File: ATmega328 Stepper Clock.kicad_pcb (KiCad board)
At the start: 2 copper layers, 9 parts, among them IC1 ATMEGA328-AU, J1 Conn_01x04_Pin, J2 SBH11-PBPC-D05-ST-BK, Y1 Crystal

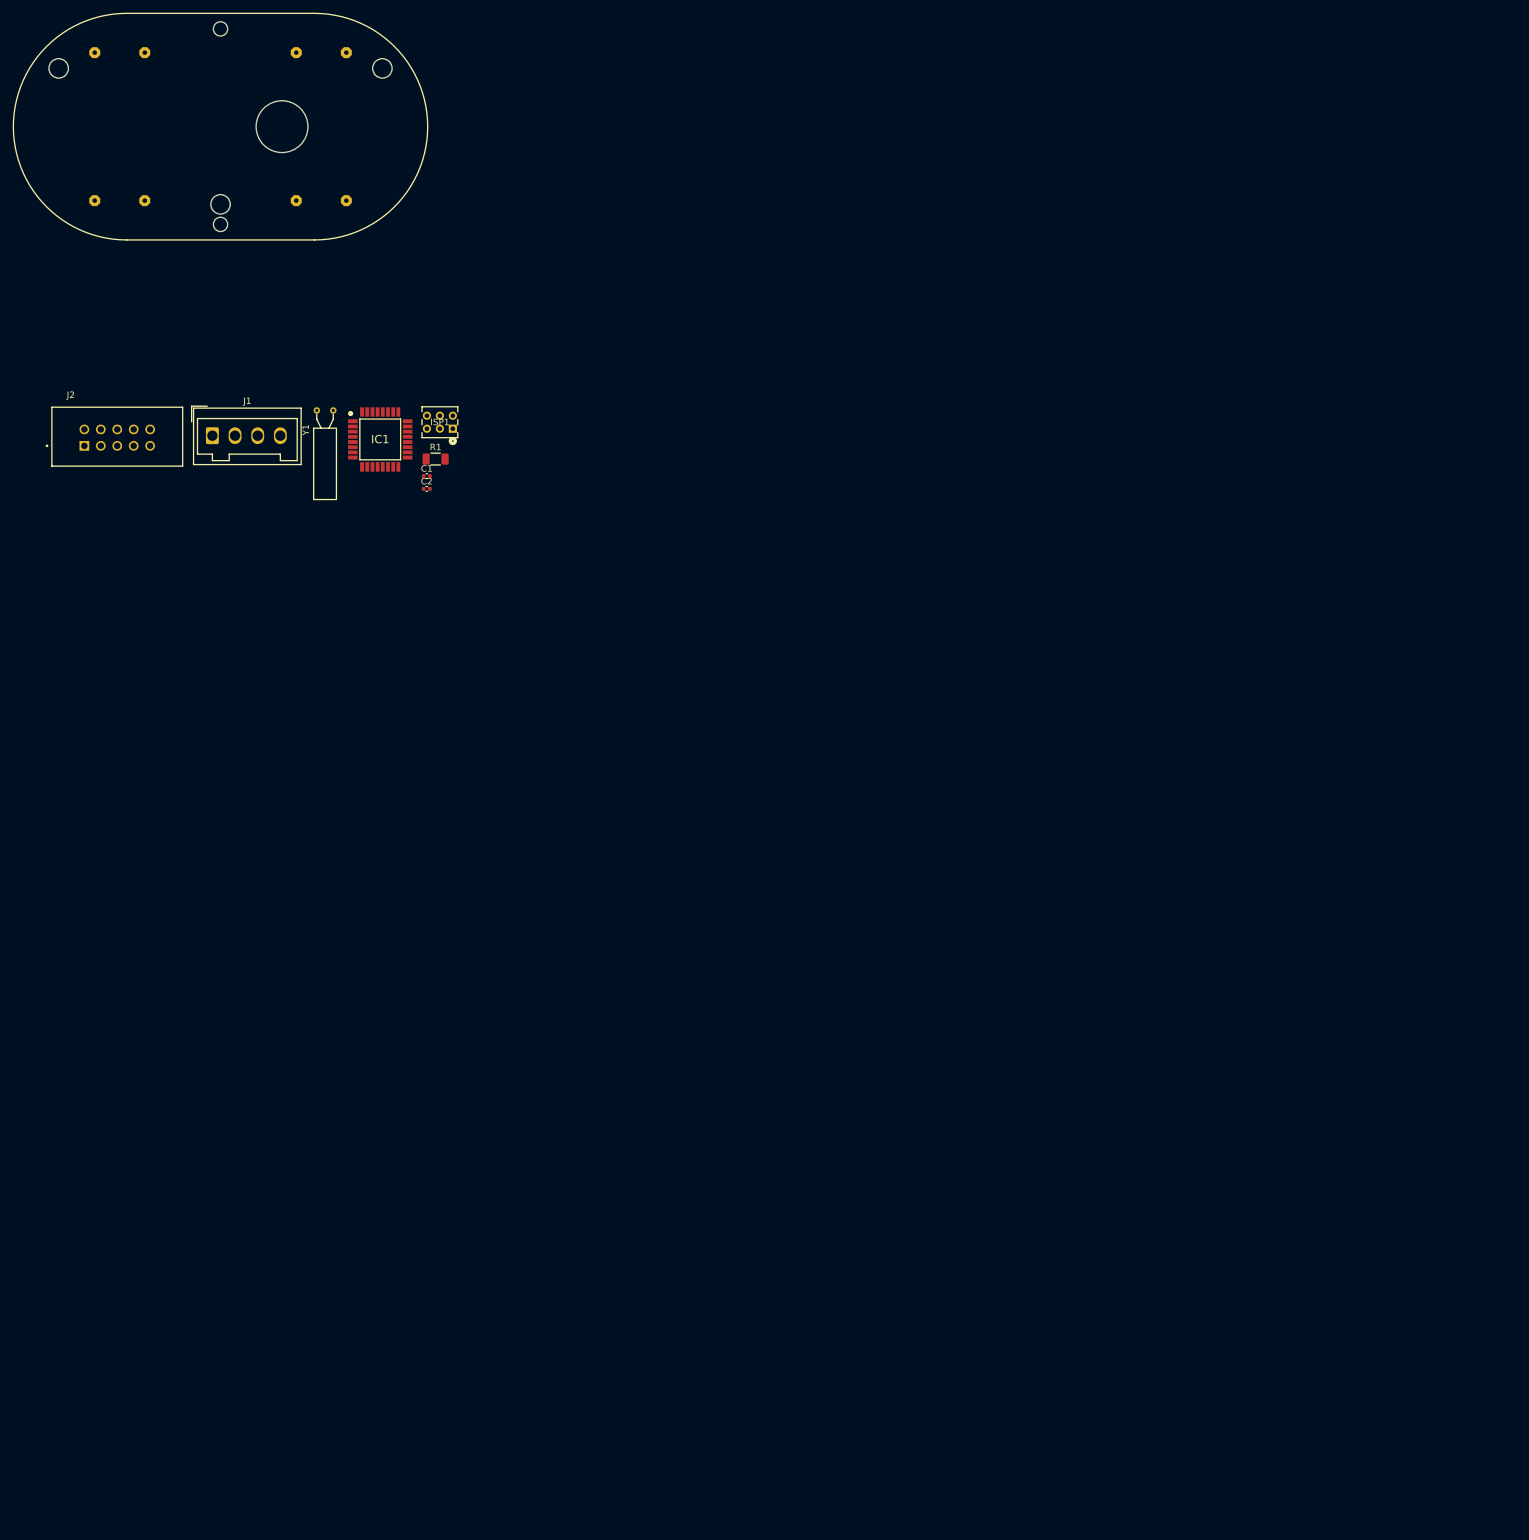
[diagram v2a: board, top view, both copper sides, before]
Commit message: changed the crystal to one which was available in the mouser website again made the PCB layout , all the SMD components are on the front and the THT are in the bottom
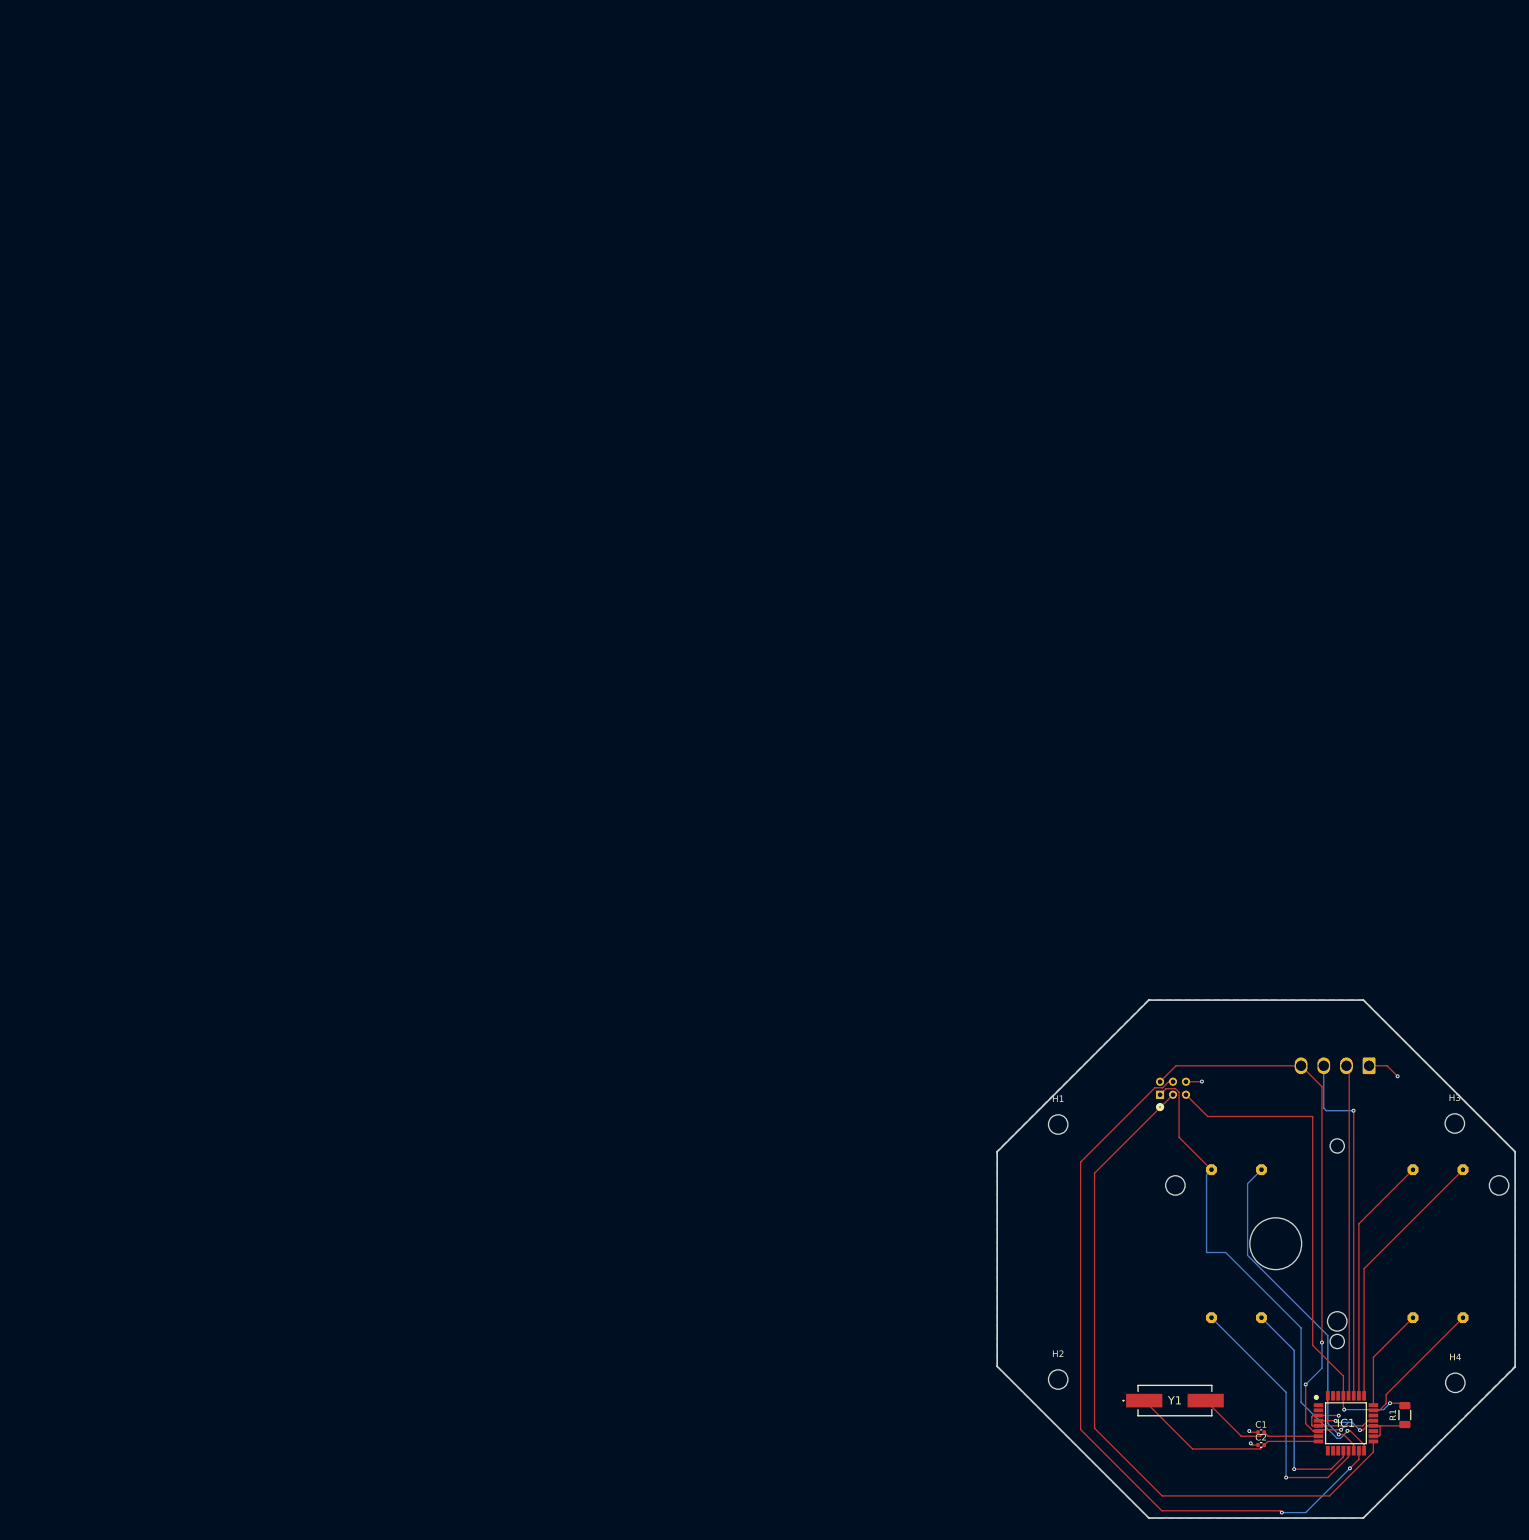
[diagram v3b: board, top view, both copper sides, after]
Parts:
- removed J2: SBH11-PBPC-D05-ST-BK, SBH11-PBPC-D05-ST-BK:SULLINS_SBH11-PBPC-D05-ST-BK
- added H1: MountingHole, MountingHole:MountingHole_3mm, F.Cu at (118.1, 70.2)
- added H2: MountingHole, MountingHole:MountingHole_3mm, F.Cu at (118.1, 109.6)
- added H3: MountingHole, MountingHole:MountingHole_3mm, F.Cu at (179.4, 70.1)
- added H4: MountingHole, MountingHole:MountingHole_3mm, F.Cu at (179.5, 110.1)
- ISP1, J1, VID28-1: moved to B.Cu
- Y1: value Crystal -> ABLS-16.000MHZ-B4-T; footprint Crystal:Crystal_AT310_D3.0mm_L10.0mm_Horizontal -> SamacSys_Parts:ABLS
- moved VID28-1 244.0 mm to (161.2, 88.6), turned to 180 degrees
- moved IC1 212.9 mm to (162.6, 116.4)
- moved R1 210.3 mm to (171.7, 115.1), turned to 90 degrees
- moved J1 203.5 mm to (166.2, 61.2), turned to 180 degrees
- moved Y1 202.4 mm to (136.2, 112.9)
- moved C1 196.0 mm to (149.5, 117.8)
- moved C2 196.0 mm to (149.5, 119.7)
- moved ISP1 153.0 mm to (135.9, 64.6), turned to 180 degrees
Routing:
- net MOSI: track 0.00 -> 113.8 mm, vias 0 -> 2
- net SCK: track 0.00 -> 108.4 mm
- net VCC: track 0.00 -> 105.9 mm, vias 0 -> 5
- net RESET: track 0.00 -> 78.2 mm, vias 0 -> 2
- net MISO&MOT_MINUTE_B: track 0.00 -> 76.0 mm, vias 0 -> 1
- net SDA: track 0.00 -> 55.4 mm, vias 0 -> 1
- net MOT_MINUTE_A: track 0.00 -> 51.5 mm, vias 0 -> 1
- net SCL: track 0.00 -> 51.2 mm
- net MOT_MINUTE_C: track 0.00 -> 41.4 mm, vias 0 -> 1
- net MOT_HOUR_A: track 0.00 -> 41.3 mm
- net MOT_HOUR_C: track 0.00 -> 38.4 mm
- net MOT_MINUTE_D: track 0.00 -> 34.8 mm, vias 0 -> 1
- net Net-(IC1-(PCINT7/XTAL2/TOSC2)_PB7): track 0.00 -> 30.5 mm
- net GND: track 0.00 -> 25.6 mm, vias 0 -> 5
- net MOT_HOUR_B: track 0.00 -> 20.6 mm
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- added copper zone on B.Cu, net GND
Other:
- board outline added: 80 x 80 mm
